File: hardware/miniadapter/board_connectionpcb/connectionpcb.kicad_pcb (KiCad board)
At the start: 2 copper layers, 10 x 6 mm, 11 parts

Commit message: new layout
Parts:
- removed TP101, TP102, TP103, TP104, TP105, TP106, TP107, TP108, TP109, TP110: TestPoint, TestPoint:TestPoint_Pad_1.0x1.0mm
- added J101: Conn_01x04, minipcb:minipcb_alt_boardedge, B.Cu at (101.0, 101.5)
- added J102: Conn_02x03_Odd_Even, minipcb:ESP8685-WROOM-07, B.Cu at (100.5, 98.8)
- added REF**: Tab, PCM_kikit:Tab, F.Cu at (106.2, 96.1)
- added REF**: Tab, PCM_kikit:Tab, F.Cu at (110.0, 100.0)
- added REF**: Tab, PCM_kikit:Tab, F.Cu at (106.2, 102.1)
- added REF**: Tab, PCM_kikit:Tab, F.Cu at (100.0, 100.0)
- AE101: footprint Capacitor_SMD:C_0603_1608Metric_Pad1.08x0.95mm_HandSolder -> Capacitor_SMD:C_0603_1608Metric
- moved AE101 7.01 mm to (101.5, 96.8), turned to 180 degrees
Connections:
- AE101 pad 1: /ANT -> unconnected-(AE101-A-Pad1)
- AE101 pad 2: /GND -> unconnected-(AE101-Shield-Pad2)
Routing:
- net unconnected-(AE101-Shield-Pad2): track 0.00 -> 11.0 mm, vias 0 -> 2
- net /GND: track 10.8 -> 0.00 mm, vias 24 -> 0
- net Net-(TP105-Pad1): track 6.58 -> 0.00 mm, vias 2 -> 0
- net /IO5: track 0.00 -> 6.04 mm, vias 0 -> 2
- added copper zone on B.Cu, net unconnected-(AE101-Shield-Pad2)
- added copper zone on F.Cu, net unconnected-(AE101-Shield-Pad2)
- removed copper zone on B.Cu, net /GND
- removed copper zone on F.Cu, net /GND
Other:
- outline, holes or cut-outs redrawn

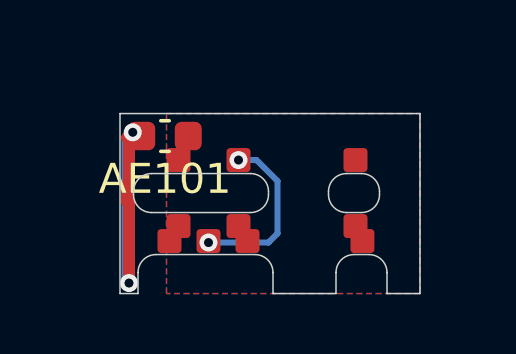
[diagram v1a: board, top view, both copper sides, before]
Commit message: layout changes and panel generation
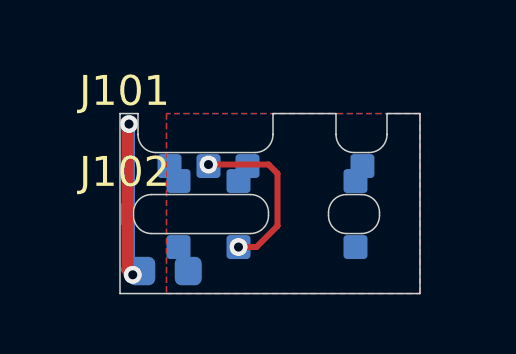
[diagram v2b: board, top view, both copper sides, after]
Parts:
- AE101, REF** (x4): moved to B.Cu
- J101, J102: moved to F.Cu
- moved REF** 6.00 mm to (106.2, 102.1), turned to 90 degrees
- moved REF** 6.00 mm to (106.2, 96.1), turned to -90 degrees
- moved J101 4.70 mm to (101.0, 96.8)
- moved AE101 4.50 mm to (101.5, 101.3)
- moved REF** 1.80 mm to (110.0, 98.2)
- moved REF** 1.80 mm to (100.0, 98.2)
- moved J102 0.70 mm to (100.5, 99.5)
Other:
- outline, holes or cut-outs redrawn
